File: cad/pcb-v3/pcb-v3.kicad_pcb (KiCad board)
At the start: 4 copper layers, 19.3 x 19.3 mm, 46 parts

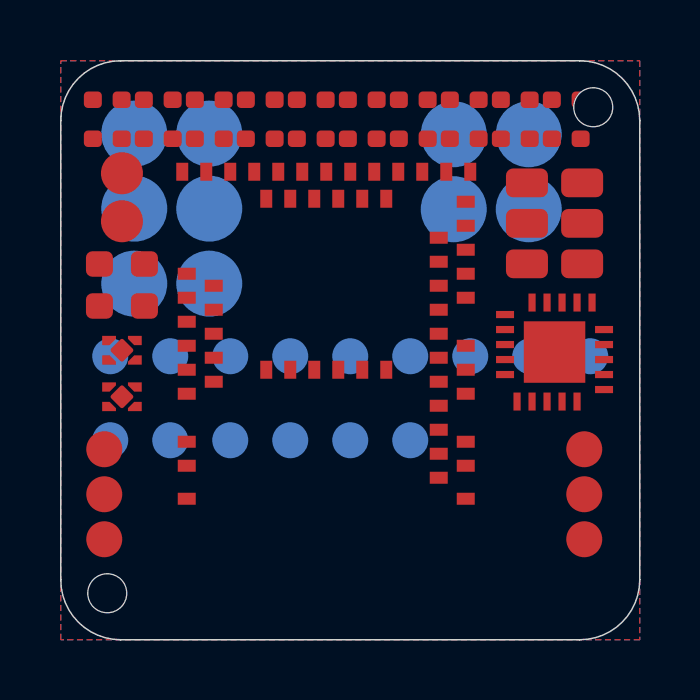
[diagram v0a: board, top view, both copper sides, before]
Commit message: Second pass: B1 closed by two-source cross-validation, pcb-v3 built, blocked list updated
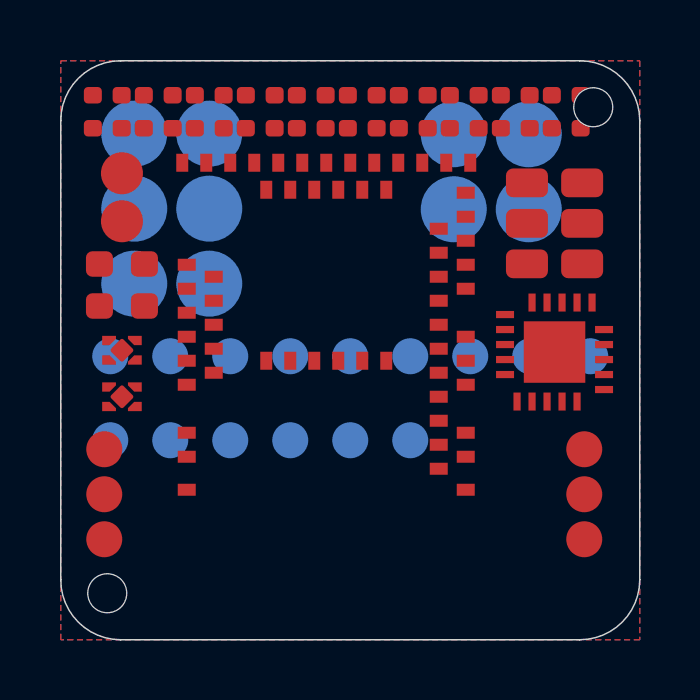
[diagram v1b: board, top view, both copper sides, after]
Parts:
- moved C10 0.35 mm to (0.40, -7.40)
- moved C12 0.35 mm to (2.10, -7.40)
- moved C13 0.35 mm to (3.80, -7.40)
- moved C3 0.35 mm to (-8.10, -7.40)
- moved C4 0.35 mm to (-6.40, -7.40)
- moved C6 0.35 mm to (-4.70, -7.40)
- moved C8 0.35 mm to (-3.00, -7.40)
- moved C9 0.35 mm to (-1.30, -7.40)
- moved R1 0.35 mm to (5.50, -7.40)
- moved R2 0.35 mm to (7.20, -7.40)
- moved U1 0.30 mm to (-0.80, 0.90)
- moved R3 0.15 mm to (-8.10, -8.50)
- moved R4 0.15 mm to (-6.40, -8.50)
- moved R5 0.15 mm to (-4.70, -8.50)
- moved R6 0.15 mm to (-3.00, -8.50)
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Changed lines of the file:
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@@
 	(footprint "touchid:U1"
 		(layer "F.Cu")
-		(at -0.8 1.2)
+		(at -0.8 0.9)
 		(property "Reference" "U1"
 			(at 0 0 0)
@@
 	(footprint "touchid:C3"
 		(layer "F.Cu")
-		(at -8.1 -7.05)
+		(at -8.1 -7.4)
 		(property "Reference" "C3"
 			(at 0 0 0)
@@
 	(footprint "touchid:C4"
 		(layer "F.Cu")
-		(at -6.4 -7.05)
+		(at -6.4 -7.4)
 		(property "Reference" "C4"
 			(at 0 0 0)
@@
 	(footprint "touchid:C6"
 		(layer "F.Cu")
-		(at -4.7 -7.05)
+		(at -4.7 -7.4)
 		(property "Reference" "C6"
 			(at 0 0 0)
@@
 	(footprint "touchid:C8"
 		(layer "F.Cu")
-		(at -3.0 -7.05)
+		(at -3.0 -7.4)
 		(property "Reference" "C8"
 			(at 0 0 0)
@@
 	(footprint "touchid:C9"
 		(layer "F.Cu")
-		(at -1.3 -7.05)
+		(at -1.3 -7.4)
 		(property "Reference" "C9"
 			(at 0 0 0)
@@
 	(footprint "touchid:C10"
 		(layer "F.Cu")
-		(at 0.4 -7.05)
+		(at 0.4 -7.4)
 		(property "Reference" "C10"
 			(at 0 0 0)
@@
 	(footprint "touchid:C12"
 		(layer "F.Cu")
-		(at 2.1 -7.05)
+		(at 2.1 -7.4)
 		(property "Reference" "C12"
 			(at 0 0 0)
@@
 	(footprint "touchid:C13"
 		(layer "F.Cu")
-		(at 3.8 -7.05)
+		(at 3.8 -7.4)
 		(property "Reference" "C13"
 			(at 0 0 0)
@@
 	(footprint "touchid:R1"
 		(layer "F.Cu")
-		(at 5.5 -7.05)
+		(at 5.5 -7.4)
 		(property "Reference" "R1"
 			(at 0 0 0)
@@
 	(footprint "touchid:R2"
 		(layer "F.Cu")
-		(at 7.2 -7.05)
+		(at 7.2 -7.4)
 		(property "Reference" "R2"
 			(at 0 0 0)
@@
 	(footprint "touchid:R3"
 		(layer "F.Cu")
-		(at -8.1 -8.35)
+		(at -8.1 -8.5)
 		(property "Reference" "R3"
 			(at 0 0 0)
@@
 	(footprint "touchid:R4"
 		(layer "F.Cu")
-		(at -6.4 -8.35)
+		(at -6.4 -8.5)
 		(property "Reference" "R4"
 			(at 0 0 0)
@@
 	(footprint "touchid:R5"
 		(layer "F.Cu")
-		(at -4.7 -8.35)
+		(at -4.7 -8.5)
 		(property "Reference" "R5"
 			(at 0 0 0)
@@
 	(footprint "touchid:R6"
 		(layer "F.Cu")
-		(at -3.0 -8.35)
+		(at -3.0 -8.5)
 		(property "Reference" "R6"
 			(at 0 0 0)
@@
 	(footprint "touchid:R7"
 		(layer "F.Cu")
-		(at -1.3 -8.35)
+		(at -1.3 -8.5)
 		(property "Reference" "R7"
 			(at 0 0 0)
@@
 	(footprint "touchid:ROV1"
 		(layer "F.Cu")
-		(at 0.4 -8.35)
+		(at 0.4 -8.5)
 		(property "Reference" "ROV1"
 			(at 0 0 0)
@@
 	(footprint "touchid:ROV2"
 		(layer "F.Cu")
-		(at 2.1 -8.35)
+		(at 2.1 -8.5)
 		(property "Reference" "ROV2"
 			(at 0 0 0)
@@
 	(footprint "touchid:ROK1"
 		(layer "F.Cu")
-		(at 3.8 -8.35)
+		(at 3.8 -8.5)
 		(property "Reference" "ROK1"
 			(at 0 0 0)
@@
 	(footprint "touchid:ROK2"
 		(layer "F.Cu")
-		(at 5.5 -8.35)
+		(at 5.5 -8.5)
 		(property "Reference" "ROK2"
 			(at 0 0 0)
@@
 	(footprint "touchid:ROK3"
 		(layer "F.Cu")
-		(at 7.2 -8.35)
+		(at 7.2 -8.5)
 		(property "Reference" "ROK3"
 			(at 0 0 0)
@@
 		(polygon
 			(pts
-				(xy -7.05 5.1499999999999995)
-				(xy 5.45 5.1499999999999995)
+				(xy -7.05 4.85)
+				(xy 5.45 4.85)
 				(xy 5.45 9.65)
 				(xy -7.05 9.65)
@@
 		(polygon
 			(pts
-				(xy -7.05 5.1499999999999995)
-				(xy 5.45 5.1499999999999995)
+				(xy -7.05 4.85)
+				(xy 5.45 4.85)
 				(xy 5.45 9.65)
 				(xy -7.05 9.65)
@@
 		(polygon
 			(pts
-				(xy -7.05 5.1499999999999995)
-				(xy 5.45 5.1499999999999995)
+				(xy -7.05 4.85)
+				(xy 5.45 4.85)
 				(xy 5.45 9.65)
 				(xy -7.05 9.65)
@@
 		(polygon
 			(pts
-				(xy -7.05 5.1499999999999995)
-				(xy 5.45 5.1499999999999995)
+				(xy -7.05 4.85)
+				(xy 5.45 4.85)
 				(xy 5.45 9.65)
 				(xy -7.05 9.65)

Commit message: Screw bosses are hard constraints: drawn as keep-outs on all 4 layers, 0402s packed by search, 20/20 placed
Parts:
- moved ROK2 17.1 mm to (-6.90, 3.30), turned to 90 degrees
- moved ROK1 16.7 mm to (6.50, 7.98)
- moved ROK3 13.6 mm to (6.15, 5.10), turned to 90 degrees
- moved R1 13.6 mm to (-8.10, -7.42)
- moved R2 13.4 mm to (-6.15, -7.42)
- moved ROV2 12.5 mm to (5.50, 3.58)
- moved ROV1 4.97 mm to (5.25, -7.42)
- moved R7 4.77 mm to (3.35, -7.42)
- moved R6 4.58 mm to (1.45, -7.42)
- moved R5 4.39 mm to (-0.45, -7.42)
- moved R4 4.19 mm to (-2.35, -7.42)
- moved R3 4.00 mm to (-4.25, -7.42)
- moved C13 1.83 mm to (5.25, -8.52)
- moved C12 1.68 mm to (3.35, -8.52)
- moved C10 1.54 mm to (1.45, -8.52)
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
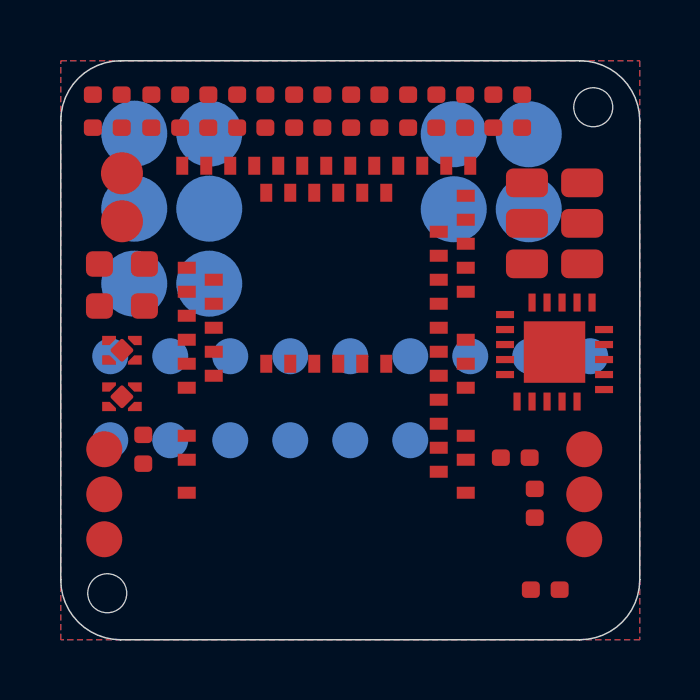
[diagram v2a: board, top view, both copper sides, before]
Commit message: Fix the KiCad freeze: GND pours read as board-wide obstacles; route first, pour last. Add ROUTING-SETTINGS.md
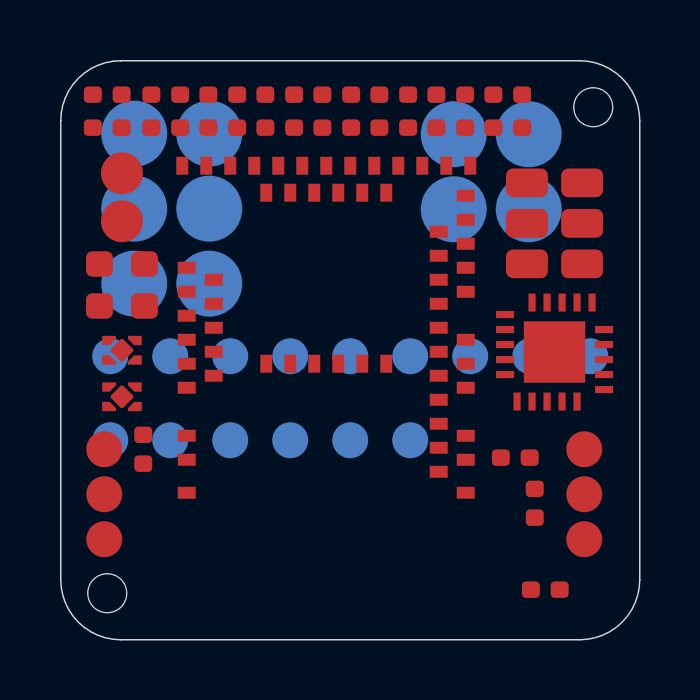
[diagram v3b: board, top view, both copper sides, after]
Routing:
- removed copper zone on B.Cu, net GND
- removed copper zone on F.Cu, net GND
- removed copper zone on In2.Cu, net GND
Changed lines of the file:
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@@
-		)
-	)
-	(zone
-		(net 3)
-		(net_name "GND")
-		(layers "F.Cu")
-		(name "GND_F_Cu")
-		(hatch edge 0.5)
-		(connect_pads (clearance 0.2))
-		(min_thickness 0.25)
-		(fill yes (thermal_gap 0.3) (thermal_bridge_width 0.3))
-		(polygon
-			(pts
-				(xy -9.65 -9.65)
-				(xy 9.65 -9.65)
-				(xy 9.65 9.65)
-				(xy -9.65 9.65)
-			)
-		)
-	)
-	(zone
-		(net 3)
-		(net_name "GND")
-		(layers "In2.Cu")
-		(name "GND_In2_Cu")
-		(hatch edge 0.5)
-		(connect_pads (clearance 0.2))
-		(min_thickness 0.25)
-		(fill yes (thermal_gap 0.3) (thermal_bridge_width 0.3))
-		(polygon
-			(pts
-				(xy -9.65 -9.65)
-				(xy 9.65 -9.65)
-				(xy 9.65 9.65)
-				(xy -9.65 9.65)
-			)
-		)
-	)
-	(zone
-		(net 3)
-		(net_name "GND")
-		(layers "B.Cu")
-		(name "GND_B_Cu")
-		(hatch edge 0.5)
-		(connect_pads (clearance 0.2))
-		(min_thickness 0.25)
-		(fill yes (thermal_gap 0.3) (thermal_bridge_width 0.3))
-		(polygon
-			(pts
-				(xy -9.65 -9.65)
-				(xy 9.65 -9.65)
-				(xy 9.65 9.65)
-				(xy -9.65 9.65)
-			)
 		)
 	)

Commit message: pcb-v3: fix the two routing root causes (43 dead module pads sealing the ring; area-only packing at 0.34mm). Add check_escape.py gate. 14/27 -> 23/27 nets, but router still escalates below the fab floor.
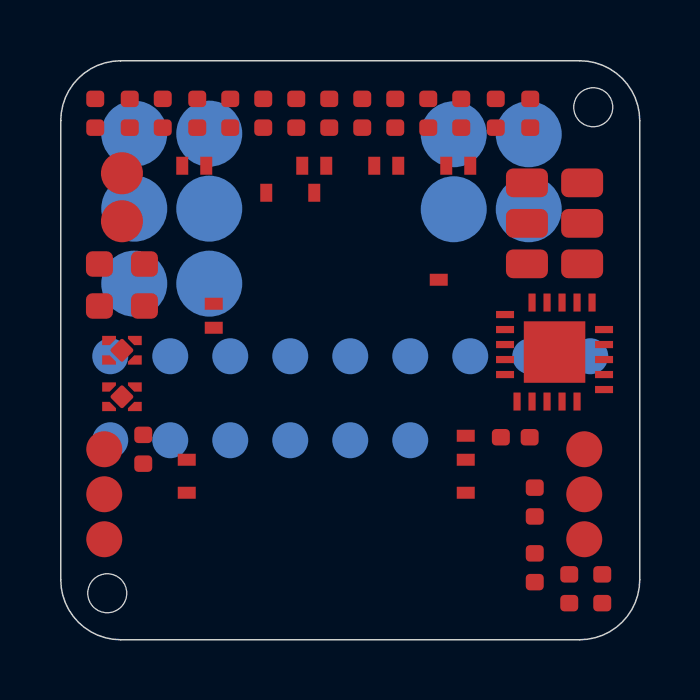
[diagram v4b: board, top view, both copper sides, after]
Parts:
- moved C6 18.9 mm to (6.15, 7.25), turned to 90 degrees
- moved C4 16.3 mm to (5.50, 2.90)
- moved ROK2 14.9 mm to (7.30, 7.95)
- moved C8 12.7 mm to (-6.90, 3.30), turned to 90 degrees
- moved C13 11.5 mm to (-6.25, -7.90), turned to 90 degrees
- moved ROV2 11.5 mm to (6.00, -7.90), turned to 90 degrees
- moved C12 10.7 mm to (-7.35, -7.90), turned to 90 degrees
- moved R2 8.76 mm to (2.60, -7.90), turned to 90 degrees
- moved R5 8.06 mm to (-8.50, -7.90), turned to 90 degrees
- moved R1 7.42 mm to (-0.70, -7.90), turned to 90 degrees
- moved C10 5.49 mm to (-4.00, -7.90), turned to 90 degrees
- moved C3 5.24 mm to (-2.90, -7.90), turned to 90 degrees
- moved R7 2.99 mm to (0.40, -7.90), turned to 90 degrees
- moved R4 2.79 mm to (-5.10, -7.90), turned to 90 degrees
- moved R3 2.50 mm to (-1.80, -7.90), turned to 90 degrees
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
